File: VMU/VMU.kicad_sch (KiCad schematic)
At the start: 19 parts, among them J1 Conn_01x04_Pin, J10 Conn_01x03_Pin, J11 Conn_01x03_Pin, J12 Conn_01x04_Pin, J13 Conn_01x04_Pin, J14 Conn_01x06_Pin, J16 Conn_01x02_Pin, J2 Conn_01x03_Pin, J3 Conn_01x03_Pin, J4 Conn_01x03_Pin, J5 Conn_01x03_Pin, J6 Conn_01x03_Pin, J7 Conn_01x08_Pin, J8 Conn_01x08_Pin, J9 Conn_01x03_Pin, U1 TLV9064, U2 TLV9064

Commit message: sdfsd
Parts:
- removed J1, J12, J13: Conn_01x04_Pin, KTHFS:Wurth-WTB_2.54_male_angle_4, symbol Connector:Conn_01x04_Pin
- removed J10, J11, J2, J3, J4, J5, J6, J9: Conn_01x03_Pin, KTHFS:Wurth-WBT_2.54_male_angle_3, symbol Connector:Conn_01x03_Pin
- removed J14: Conn_01x06_Pin, KTHFS:Wurth-WBT_2.54_male_angle_6, symbol Connector:Conn_01x06_Pin
- added J1, J2, J3, J4: TBL009-254-14GY-2GY, KTHFS:TBL00925414GY2GY, symbol realTBL009-254-14GY-2GY:TBL009-254-14GY-2GY
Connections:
- net ANALOG_1_SIGNAL: now also J1.3, J1.4
- net ANALOG_2_SIGNAL: now also J1.10, J1.9
- net ANALOG_3_SIGNAL: now also J1.15, J1.16
- net ANALOG_4_SIGNAL: now also J1.21, J1.22
- net ANALOG_5_SIGNAL: now also J2.3, J2.4
- net ANALOG_6_SIGNAL: now also J2.10, J2.9
- net ANALOG_7_SIGNAL: now also J2.15, J2.16
- net ANALOG_8_SIGNAL: now also J2.21, J2.22
- net CAN1_H: now also J4.3, J4.4
- net CAN1_L: now also J4.5, J4.6
- net DIGITAL_SUPPLY_1: now also J3.5, J3.6
- net DIGITAL_SUPPLY_2: now also J3.19, J3.20
- net DIGITAL_SUPPLY_3: now also J4.13, J4.14
- net GND: now also J1.11, J1.12, J1.17, J1.18, J1.23, J1.24, J1.27, J1.28, J1.5, J1.6, J2.11, J2.12, J2.17, J2.18, J2.23, J2.24, J2.27, J2.28, J2.5, J2.6, J3.11, J3.12, J3.13, J3.14, J3.25, J3.26, J3.27, J3.28, J4.23, J4.24, J4.25, J4.26, J4.27, J4.28, J4.7, J4.8
- net I2C_SCL: now also J3.10, J3.9
- net I2C_SDA: now also J3.7, J3.8
- net SPI_MISO: now also J4.15, J4.16
- net SPI_MOSI: now also J4.17, J4.18
- net SPI_SCLK: now also J4.19, J4.20
- net SPI_~{CS}: now also J4.21, J4.22
- net SUPPLY_1: now also J1.1, J1.2
- net SUPPLY_2: now also J1.7, J1.8
- net SUPPLY_3: now also J1.13, J1.14
- net SUPPLY_4: now also J1.19, J1.20
- net SUPPLY_5: now also J2.1, J2.2
- net SUPPLY_6: now also J2.7, J2.8
- net SUPPLY_7: now also J2.13, J2.14
- net SUPPLY_8: now also J2.19, J2.20
- net UART_RX: now also J3.21, J3.22
- net UART_TX: now also J3.23, J3.24
- net battery_in: now also J4.1, J4.2
- new net GPIO_SPLY_1: J2.25, J2.26
- new net GPIO_SPLY_2: J1.25, J1.26
- new net GPIO_SPLY_3: J4.11, J4.12
- new net GPIO_SPLY_4: J4.10, J4.9
- new net GPIO_SPLY_5: J3.1, J3.2
- new net GPIO_SPLY_6: J3.3, J3.4
- new net GPIO_SPLY_7: J3.15, J3.16
- new net GPIO_SPLY_8: J3.17, J3.18
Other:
- sheet MCU ports: added GPIO_SPLY_1, GPIO_SPLY_2, GPIO_SPLY_3, GPIO_SPLY_4, GPIO_SPLY_5, GPIO_SPLY_6, GPIO_SPLY_7, GPIO_SPLY_8; removed none
- note removed: "I/O"
- note removed: "I/O SENSORS"
- moved on the sheet: C?, J16, J7, J8, U1A, U1B, U1C, U1D, U1E, U2A, U2B, U2C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

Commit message: RoutingV2
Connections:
- net ANALOG_1_SIGNAL: now also J1.25, J1.26; no longer J1.3, J1.4
- net ANALOG_2_SIGNAL: now also J1.19, J1.20; no longer J1.10, J1.9
- net ANALOG_3_SIGNAL: now also J1.13, J1.14; no longer J1.15, J1.16
- net ANALOG_4_SIGNAL: now also J1.7, J1.8; no longer J1.21, J1.22
- net ANALOG_5_SIGNAL: now also J2.25, J2.26; no longer J2.3, J2.4
- net ANALOG_6_SIGNAL: now also J2.19, J2.20; no longer J2.10, J2.9
- net ANALOG_7_SIGNAL: now also J2.13, J2.14; no longer J2.15, J2.16
- net ANALOG_8_SIGNAL: now also J2.7, J2.8; no longer J2.21, J2.22
- net CAN1_H: now also J4.25, J4.26; no longer J4.3, J4.4
- net CAN1_L: now also J4.23, J4.24; no longer J4.5, J4.6
- net DIGITAL_SUPPLY_3: now also J4.15, J4.16; no longer J4.13, J4.14
- net GND: now also J1.1, J1.2, J2.1, J2.2, J4.1, J4.2, J4.21, J4.22, J4.3, J4.4, J4.5, J4.6; no longer J1.27, J1.28, J2.27, J2.28, J4.23, J4.24, J4.25, J4.26, J4.27, J4.28, J4.7, J4.8
- net GPIO_SPLY_1: now also J2.3, J2.4; no longer J2.25, J2.26
- net GPIO_SPLY_2: now also J1.3, J1.4; no longer J1.25, J1.26
- net GPIO_SPLY_3: now also J4.17, J4.18; no longer J4.11, J4.12
- net GPIO_SPLY_4: now also J4.19, J4.20; no longer J4.10, J4.9
- net SPI_MISO: now also J4.13, J4.14; no longer J4.15, J4.16
- net SPI_MOSI: now also J4.11, J4.12; no longer J4.17, J4.18
- net SPI_SCLK: now also J4.10, J4.9; no longer J4.19, J4.20
- net SPI_~{CS}: now also J4.7, J4.8; no longer J4.21, J4.22
- net SUPPLY_1: now also J1.27, J1.28; no longer J1.1, J1.2
- net SUPPLY_2: now also J1.21, J1.22; no longer J1.7, J1.8
- net SUPPLY_3: now also J1.15, J1.16; no longer J1.13, J1.14
- net SUPPLY_4: now also J1.10, J1.9; no longer J1.19, J1.20
- net SUPPLY_5: now also J2.27, J2.28; no longer J2.1, J2.2
- net SUPPLY_6: now also J2.21, J2.22; no longer J2.7, J2.8
- net SUPPLY_7: now also J2.15, J2.16; no longer J2.13, J2.14
- net SUPPLY_8: now also J2.10, J2.9; no longer J2.19, J2.20
- net battery_in: now also J4.27, J4.28; no longer J4.1, J4.2

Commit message: fiixes
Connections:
- net +5V: now also J4.4, J4.6
- net GND: no longer J4.4, J4.6
- net GPIO_SPLY_4 renamed GPIO_GND_4
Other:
- sheet MCU ports: added GPIO_GND_4; removed GPIO_SPLY_4
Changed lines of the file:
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@@
   (junction (at 383.54 127.635) (diameter 0) (color 0 0 0 0)
   )
+  (junction (at 380.365 177.8) (diameter 0) (color 0 0 0 0)
+  )
   (junction (at 256.54 266.065) (diameter 0) (color 0 0 0 0)
   )
   (junction (at 383.54 109.855) (diameter 0) (color 0 0 0 0)
   )
-  (junction (at 380.365 177.8) (diameter 0) (color 0 0 0 0)
-  )
   (junction (at 279.4 250.19) (diameter 0) (color 0 0 0 0)
   )
@@
   (junction (at 295.275 177.8) (diameter 0) (color 0 0 0 0)
   )
-  (junction (at 380.365 175.26) (diameter 0) (color 0 0 0 0)
-  )
   (junction (at 298.45 109.855) (diameter 0) (color 0 0 0 0)
   )
@@
     (stroke (width 0) (type default))
   )
-  (wire (pts (xy 380.365 177.8) (xy 380.365 175.26))
-    (stroke (width 0) (type default))
-  )
   (wire (pts (xy 155.575 145.415) (xy 155.575 153.035))
     (stroke (width 0) (type default))
@@
     (stroke (width 0) (type default))
   )
-  (wire (pts (xy 380.365 180.34) (xy 380.365 177.8))
-    (stroke (width 0) (type default))
-  )
   (wire (pts (xy 227.33 131.826) (xy 231.775 131.826))
     (stroke (width 0) (type default))
@@
     (stroke (width 0) (type default))
   )
+  (wire (pts (xy 385.445 177.8) (xy 380.365 177.8))
+    (stroke (width 0) (type default))
+  )
   (wire (pts (xy 41.91 86.36) (xy 73.66 86.36))
     (stroke (width 0) (type default))
@@
     (stroke (width 0) (type default))
   )
-  (wire (pts (xy 225.425 139.065) (xy 207.01 139.065))
+  (wire (pts (xy 225.425 139.065) (xy 207.645 139.065))
     (stroke (width 0) (type default))
   )
@@
     (stroke (width 0) (type default))
   )
+  (wire (pts (xy 380.365 177.8) (xy 380.365 180.34))
+    (stroke (width 0) (type default))
+  )
   (wire (pts (xy 273.685 266.065) (xy 279.4 266.065))
     (stroke (width 0) (type default))
@@
   )
   (wire (pts (xy 177.165 189.865) (xy 181.61 189.865))
+    (stroke (width 0) (type default))
+  )
+  (wire (pts (xy 385.445 177.8) (xy 385.445 177.165))
     (stroke (width 0) (type default))
   )
@@
     (effects (font (size 1.27 1.27)) (justify left bottom))
   )
-  (label "GPIO_SPLY_4" (at 377.19 198.12 180) (fields_autoplaced)
-    (effects (font (size 1.27 1.27)) (justify right bottom))
-  )
   (label "SUPPLY_4" (at 48.26 68.58 0) (fields_autoplaced)
     (effects (font (size 1.27 1.27)) (justify left bottom))
@@
     (effects (font (size 1.27 1.27)) (justify right bottom))
   )
-  (label "GPIO_SPLY_4" (at 256.54 198.755 90) (fields_autoplaced)
+  (label "GPIO_GND_4" (at 256.54 198.755 90) (fields_autoplaced)
     (effects (font (size 1.27 1.27)) (justify left bottom))
   )
@@
     (effects (font (size 1.27 1.27)) (justify left bottom))
   )
-  (label "GPIO_SPLY_4" (at 298.45 198.12 0) (fields_autoplaced)
-    (effects (font (size 1.27 1.27)) (justify left bottom))
-  )
   (label "ANALOG_1_SIGNAL" (at 64.77 134.62 0) (fields_autoplaced)
     (effects (font (size 1.27 1.27)) (justify left bottom))
@@
     (effects (font (size 1.27 1.27)) (justify left bottom))
   )
+  (label "GPIO_GND_4" (at 377.19 198.12 180) (fields_autoplaced)
+    (effects (font (size 1.27 1.27)) (justify right bottom))
+  )
   (label "SUPPLY_8" (at 121.285 211.455 180) (fields_autoplaced)
     (effects (font (size 1.27 1.27)) (justify right bottom))
@@
     (effects (font (size 1.27 1.27)) (justify left bottom))
   )
+  (label "GPIO_GND_4" (at 298.45 198.12 0) (fields_autoplaced)
+    (effects (font (size 1.27 1.27)) (justify left bottom))
+  )
   (label "GPIO_SPLY_7" (at 377.825 112.395 180) (fields_autoplaced)
     (effects (font (size 1.27 1.27)) (justify right bottom))
@@
     (effects (font (size 1.27 1.27)) (justify left bottom))
   )
-  (label "SPI_MISO" (at 207.01 139.065 0) (fields_autoplaced)
+  (label "SPI_MISO" (at 207.645 139.065 0) (fields_autoplaced)
     (effects (font (size 1.27 1.27)) (justify left bottom))
   )
@@
     )
   )
+  (symbol (lib_id "power:+5V") (at 385.445 177.165 0) (mirror y) (unit 1)
+    (in_bom yes) (on_board yes) (dnp no)
+    (property "Reference" "#PWR029" (at 385.445 180.975 0)
+      (effects (font (size 1.27 1.27)) hide)
+    )
+    (property "Value" "+5V" (at 385.445 173.355 0)
+      (effects (font (size 1.27 1.27)))
+    )
+    (property "Footprint" "" (at 385.445 177.165 0)
+      (effects (font (size 1.27 1.27)) hide)
+    )
+    (property "Datasheet" "" (at 385.445 177.165 0)
+      (effects (font (size 1.27 1.27)) hide)
+    )
+    (pin "1")
+    (instances
+      (project "VMU"
+        (path "/a0b206d8-cab6-473c-9bbb-e8da011ef93c/00000000-0000-0000-0000-00005ef29697"
+          (reference "#PWR029") (unit 1)
+        )
+        (path "/a0b206d8-cab6-473c-9bbb-e8da011ef93c"
+          (reference "#PWR035") (unit 1)
+        )
+      )
+      (project "POWER"
+        (path "/cdd3e9f1-9c00-403f-9184-7e2f38425a2b"
+          (reference "#PWR0161") (unit 1)
+        )
+      )
+    )
+  )
   (symbol (lib_id "Amplifier_Operational:TLV9064") (at 281.94 257.81 0) (unit 5)
     (in_bom yes) (on_board yes) (dnp no) (fields_autoplaced)
@@
       (effects (font (size 1.27 1.27)) (justify left))
     )
-    (pin "GPIO_SPLY_4" input (at 256.54 182.88 270)
-      (effects (font (size 1.27 1.27)) (justify left))
-    )
     (pin "GPIO_SPLY_6" input (at 250.19 182.88 270)
       (effects (font (size 1.27 1.27)) (justify left))
@@
       (effects (font (size 1.27 1.27)) (justify left))
     )
+    (pin "GPIO_GND_4" input (at 256.54 182.88 270)
+      (effects (font (size 1.27 1.27)) (justify left))
+    )

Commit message: Update
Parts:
- renumbered J3 to J2, J8 to J3, J7 to J4, J16 to J5, J4 to J6, J2 to J7
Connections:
- net GPIO_SPLY_7 is gone; now on net GND: J2.15, J2.16
- net GPIO_SPLY_8 is gone; now on net GND: J2.17, J2.18
- net +5V: now also J2.11, J2.12, J2.13, J2.14, J6.1, J6.2, J6.3; no longer J6.6
- net GND: now also J6.6; no longer J2.11, J2.12, J2.13, J2.14, J6.1, J6.2, J6.3
- net GPIO_SPLY_1 renamed GPIO_GND_1
- net GPIO_SPLY_2 renamed GPIO_GND_2
- net GPIO_SPLY_3 renamed GPIO_GND_3
- net GPIO_SPLY_5 renamed GPIO_GND_5
- net GPIO_SPLY_6 renamed GPIO_GND_6
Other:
- sheet MCU ports: added GPIO_GND_1, GPIO_GND_2, GPIO_GND_3, GPIO_GND_5, GPIO_GND_6, GPIO_GND_7, GPIO_GND_8; removed GPIO_SPLY_1, GPIO_SPLY_2, GPIO_SPLY_3, GPIO_SPLY_5, GPIO_SPLY_6, GPIO_SPLY_7, GPIO_SPLY_8
- moved on the sheet: J1, J2, J6

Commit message: Update
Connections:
- net GND: no longer J2.15, J2.16, J2.25, J2.26
- new net +24V: J2.15, J2.16
- new net +3.3V: J2.25, J2.26
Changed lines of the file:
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@@
     (comment 3 "FSVEBECK@KTH.SE")
   )
-  (junction (at 293.37 132.715) (diameter 0) (color 0 0 0 0)
-  )
   (junction (at 180.975 172.085) (diameter 0) (color 0 0 0 0)
   )
@@
   (junction (at 381.635 187.325) (diameter 0) (color 0 0 0 0)
   )
-  (junction (at 378.46 132.715) (diameter 0) (color 0 0 0 0)
-  )
   (junction (at 256.54 266.065) (diameter 0) (color 0 0 0 0)
   )
-  (junction (at 378.46 120.015) (diameter 0) (color 0 0 0 0)
-  )
-  (junction (at 293.37 120.015) (diameter 0) (color 0 0 0 0)
-  )
   (junction (at 279.4 250.19) (diameter 0) (color 0 0 0 0)
   )
@@
     (stroke (width 0) (type default))
   )
-  (wire (pts (xy 293.37 130.175) (xy 293.37 132.715))
-    (stroke (width 0) (type default))
-  )
   (wire (pts (xy 230.505 169.926) (xy 230.505 169.545))
     (stroke (width 0) (type default))
@@
     (stroke (width 0) (type default))
   )
-  (wire (pts (xy 347.345 117.475) (xy 378.46 117.475))
+  (wire (pts (xy 347.345 117.475) (xy 379.73 117.475))
     (stroke (width 0) (type default))
   )
@@
     (stroke (width 0) (type default))
   )
-  (wire (pts (xy 378.46 117.475) (xy 378.46 120.015))
-    (stroke (width 0) (type default))
-  )
   (wire (pts (xy 86.995 95.885) (xy 112.395 95.885))
     (stroke (width 0) (type default))
@@
     (stroke (width 0) (type default))
   )
-  (wire (pts (xy 293.37 117.475) (xy 293.37 120.015))
-    (stroke (width 0) (type default))
-  )
   (wire (pts (xy 146.05 139.7) (xy 137.795 139.7))
     (stroke (width 0) (type default))
@@
     (stroke (width 0) (type default))
   )
-  (wire (pts (xy 324.485 117.475) (xy 293.37 117.475))
+  (wire (pts (xy 324.485 117.475) (xy 292.1 117.475))
     (stroke (width 0) (type default))
   )
@@
   )
   (wire (pts (xy 350.52 202.565) (xy 378.46 202.565))
-    (stroke (width 0) (type default))
-  )
-  (wire (pts (xy 378.46 130.175) (xy 378.46 132.715))
     (stroke (width 0) (type default))
   )
@@
     )
   )
+  (symbol (lib_id "power:+24V") (at 379.73 117.475 0) (unit 1)
+    (in_bom yes) (on_board yes) (dnp no)
+    (property "Reference" "#PWR034" (at 379.73 121.285 0)
+      (effects (font (size 1.27 1.27)) hide)
+    )
+    (property "Value" "+24V" (at 381.635 113.03 0)
+      (effects (font (size 1.27 1.27)))
+    )
+    (property "Footprint" "" (at 379.73 117.475 0)
+      (effects (font (size 1.27 1.27)) hide)
+    )
+    (property "Datasheet" "" (at 379.73 117.475 0)
+      (effects (font (size 1.27 1.27)) hide)
+    )
+    (pin "1")
+    (instances
+      (project "VMU"
+        (path "/a0b206d8-cab6-473c-9bbb-e8da011ef93c/00000000-0000-0000-0000-00005ef29697"
+          (reference "#PWR034") (unit 1)
+        )
+        (path "/a0b206d8-cab6-473c-9bbb-e8da011ef93c"
+          (reference "#PWR075") (unit 1)
+        )
+      )
+    )
+  )
   (symbol (lib_id "power:GND") (at 32.385 67.945 0) (mirror y) (unit 1)
     (in_bom yes) (on_board yes) (dnp no)
@@
         (path "/a0b206d8-cab6-473c-9bbb-e8da011ef93c"
           (reference "#PWR018") (unit 1)
+        )
+      )
+    )
+  )
+  (symbol (lib_id "power:+3.3V") (at 293.37 130.175 0) (unit 1)
+    (in_bom yes) (on_board yes) (dnp no)
+    (property "Reference" "#PWR037" (at 293.37 133.985 0)
+      (effects (font (size 1.27 1.27)) hide)
+    )
+    (property "Value" "+3.3V" (at 293.37 126.365 0)
+      (effects (font (size 1.27 1.27)))
+    )
+    (property "Footprint" "" (at 293.37 130.175 0)
+      (effects (font (size 1.27 1.27)) hide)
+    )
+    (property "Datasheet" "" (at 293.37 130.175 0)
+      (effects (font (size 1.27 1.27)) hide)
+    )
+    (pin "1")
+    (instances
+      (project "VMU"
+        (path "/a0b206d8-cab6-473c-9bbb-e8da011ef93c/00000000-0000-0000-0000-00005ef29697"
+          (reference "#PWR037") (unit 1)
+        )
+        (path "/a0b206d8-cab6-473c-9bbb-e8da011ef93c"
+          (reference "#PWR078") (unit 1)
         )
       )
@@
     )
   )
+  (symbol (lib_id "power:+3.3V") (at 378.46 130.175 0) (unit 1)
+    (in_bom yes) (on_board yes) (dnp no)
+    (property "Reference" "#PWR037" (at 378.46 133.985 0)
+      (effects (font (size 1.27 1.27)) hide)
+    )
+    (property "Value" "+3.3V" (at 378.46 125.73 0)
+      (effects (font (size 1.27 1.27)))
+    )
+    (property "Footprint" "" (at 378.46 130.175 0)
+      (effects (font (size 1.27 1.27)) hide)
+    )
+    (property "Datasheet" "" (at 378.46 130.175 0)
+      (effects (font (size 1.27 1.27)) hide)
+    )
+    (pin "1")
+    (instances
+      (project "VMU"
+        (path "/a0b206d8-cab6-473c-9bbb-e8da011ef93c/00000000-0000-0000-0000-00005ef29697"
+          (reference "#PWR037") (unit 1)
+        )
+        (path "/a0b206d8-cab6-473c-9bbb-e8da011ef93c"
+          (reference "#PWR077") (unit 1)
+        )
+      )
+    )
+  )
   (symbol (lib_id "power:GND") (at 118.745 83.185 0) (mirror y) (unit 1)
     (in_bom yes) (on_board yes) (dnp no)
@@
         )
       )
+    )
+  )
+  (symbol (lib_id "power:+24V") (at 292.1 117.475 0) (unit 1)
+    (in_bom yes) (on_board yes) (dnp no)
+    (property "Reference" "#PWR034" (at 292.1 121.285 0)
+      (effects (font (size 1.27 1.27)) hide)
+    )
+    (property "Value" "+24V" (at 288.925 114.3 0)
+      (effects (font (size 1.27 1.27)))
+    )
+    (property "Footprint" "" (at 292.1 117.475 0)
+      (effects (font (size 1.27 1.27)) hide)
+    )
+    (property "Datasheet" "" (at 292.1 117.475 0)
+      (effects (font (size 1.27 1.27)) hide)
+    )
+    (pin "1")
+    (instances
+      (project "VMU"
+        (path "/a0b206d8-cab6-473c-9bbb-e8da011ef93c/00000000-0000-0000-0000-00005ef29697"
+          (reference "#PWR034") (unit 1)
+        )
+        (path "/a0b206d8-cab6-473c-9bbb-e8da011ef93c"
+          (reference "#PWR076") (unit 1)
+        )
+      )

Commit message: banana
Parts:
- removed C? (x2): 100n, Capacitor_SMD:C_0603_1608Metric_Pad1.08x0.95mm_HandSolder, symbol Device:C
- removed J2, J6: TBL009-254-14GY-2GY, KTHFS:TBL00925414GY2GY, symbol realTBL009-254-14GY-2GY:TBL009-254-14GY-2GY
- removed unit 5 of U1
- removed unit 5 of U2
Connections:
- net MCU/ANALOG_1: no longer names the net of U1.1
- net MCU/ANALOG_1: no longer U1.2 (-)
- net MCU/ANALOG_2: no longer names the net of U1.6 (-)
- net MCU/ANALOG_2: no longer U1.7
- net MCU/ANALOG_3: no longer names the net of U1.8
- net MCU/ANALOG_3: no longer U1.9 (-)
- net MCU/ANALOG_4: no longer names the net of U1.13 (-)
- net MCU/ANALOG_4: no longer U1.14
- net MCU/ANALOG_5: no longer names the net of U2.1
- net MCU/ANALOG_5: no longer U2.2 (-)
- net MCU/ANALOG_6: no longer names the net of U2.6 (-)
- net MCU/ANALOG_6: no longer U2.7
- net MCU/ANALOG_7: no longer names the net of U2.8
- net MCU/ANALOG_7: no longer U2.9 (-)
- net MCU/ANALOG_8: no longer names the net of U2.13 (-)
- net MCU/ANALOG_8: no longer U2.14
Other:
- removed sheet MCU
- sheet POWER ports: added none; removed SUPPLY_1
- note removed: "OP AMP SUPPLY"
- note removed: "To rear distribution board right"

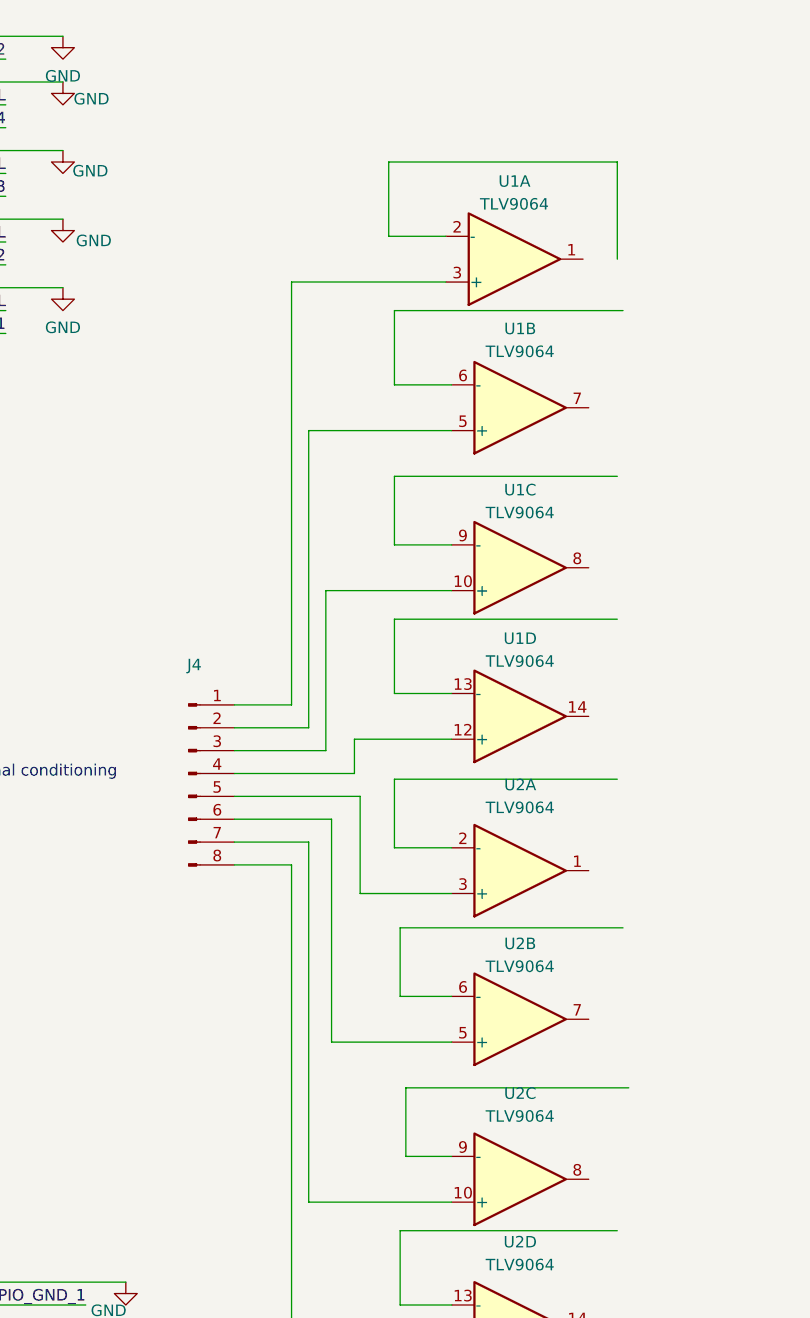
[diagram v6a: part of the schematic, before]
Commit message: Update VMU.kicad_sch
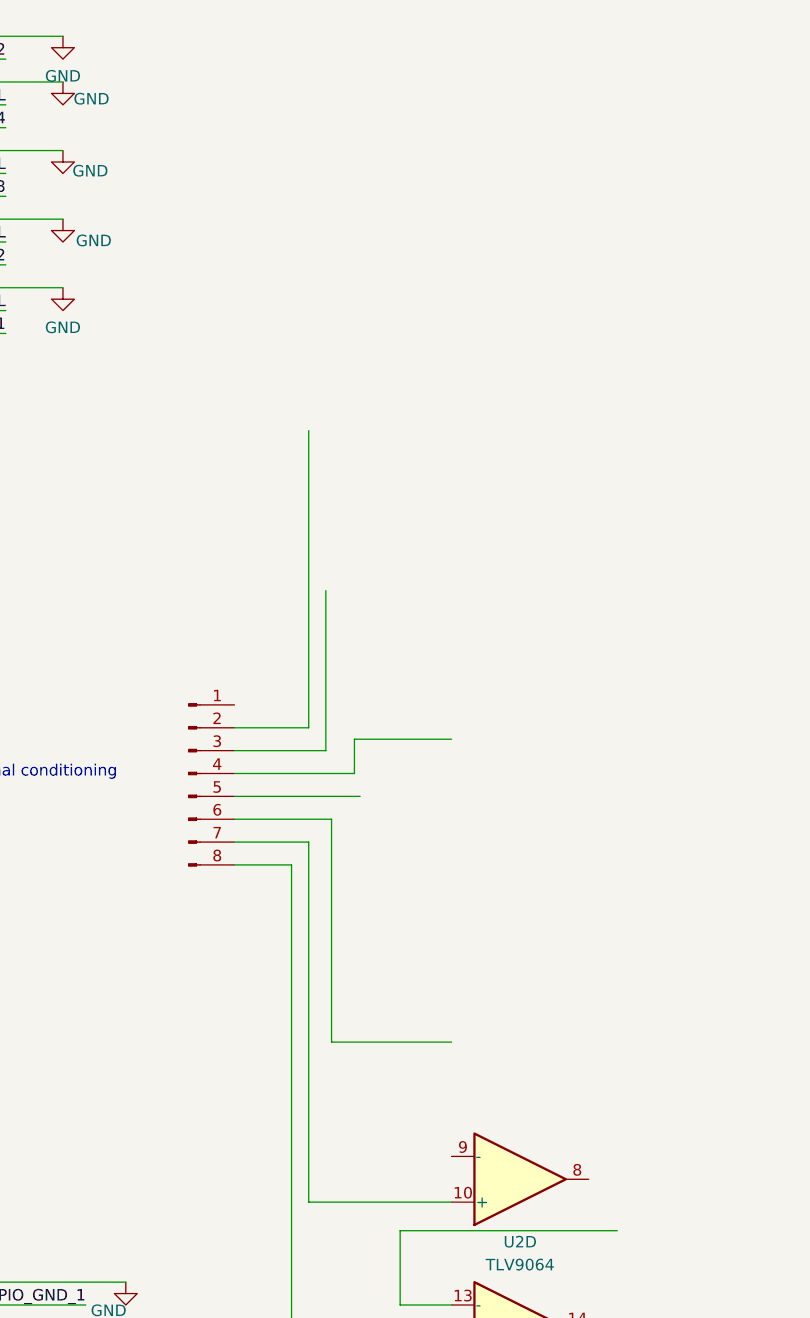
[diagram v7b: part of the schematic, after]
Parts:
- removed U1: TLV9064, Package_SO:SOIC-14_3.9x8.7mm_P1.27mm, symbol Amplifier_Operational:TLV9064
- removed unit 1 of U2
- removed unit 2 of U2
